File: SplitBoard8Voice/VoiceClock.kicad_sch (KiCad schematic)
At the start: 24 parts, among them U1001 74HC595, U1002 74HC595, U1003 4017, U1004 4017, U1005 4071

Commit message: 8 voice schematics start
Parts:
- removed JP1001: B17, Jumper:SolderJumper-2_P1.3mm_Bridged_Pad1.0x1.5mm, symbol Jumper:SolderJumper_2_Bridged
- removed JP1002: B16, Jumper:SolderJumper-2_P1.3mm_Open_Pad1.0x1.5mm, symbol Jumper:SolderJumper_2_Open
- removed U1001: 74HC595, Package_SO:SOIC-16_3.9x9.9mm_P1.27mm, symbol 74xx:74HC595
- removed U1003, U1004: 4017, Package_SO:SOIC-16_3.9x9.9mm_P1.27mm, symbol 4xxx:4017
- removed U1005: 4071, Package_SO:SOIC-14_3.9x8.7mm_P1.27mm, symbol 4xxx:4071
- added R1013, R1014, R1015, R1016: 22R, Resistor_SMD:R_0805_2012Metric, symbol Device:R_US
- added U1001, U1003: 4013, symbol 4xxx:4013
- added U1004: 74LS08, symbol 74xx:74LS08
- added U1005: 74HC595, Package_SO:SOIC-16_3.9x9.9mm_P1.27mm, symbol 74xx:74HC595
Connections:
- net +3.3V: now also U1001.14 (VDD), U1003.14 (VDD), U1004.14 (VCC), U1005.10 (~{SRCLR}), U1005.16 (VCC)
- net GND: now also U1001.6 (S), U1001.7 (VSS), U1001.8 (S), U1003.6 (S), U1003.7 (VSS), U1004.7 (GND), U1005.13 (~{OE}), U1005.8 (GND)
- net PITCH_MOSI: now also U1004.12, U1004.4; no longer U1002.14 (SER)
- net PITCH_RST_GPIO: now also U1001.10 (R), U1001.4 (R), U1003.4 (R)
- net PITCH_SCK: now also U1001.3 (C), U1004.1, U1004.9; no longer U1002.11 (SRCLK)
- net V1_CLK1: now also R1016.2; no longer R1011.2
- net V1_CLK2: now also R1015.2; no longer R1010.2
- net V2_CLK1: now also R1014.2; no longer R1012.2
- net V2_CLK2: now also R1013.2; no longer R1009.2
- net V3_CLK1: now also R1012.2; no longer R1008.2
- net V3_CLK2: now also R1011.2; no longer R1007.2
- net V4_CLK1: now also R1010.2; no longer R1006.2
- net V4_CLK2: now also R1009.2; no longer R1005.2
- net V5_CLK1: now also R1008.2; no longer R1004.2
- net V5_CLK2: now also R1007.2; no longer R1003.2
- net V6_CLK1: now also R1006.2; no longer R1002.2
- net V6_CLK2: now also R1005.2; no longer R1001.2
- net at R1011.1: now also U1005.2 (QC)
- net at R1009.1: now also U1005.15 (QA)
- net at R1012.1: now also U1005.3 (QD)
- net at R1010.1: now also U1005.1 (QB)
- net PITCH_SS renamed SR1_LATCH
- net SR1_LATCH: now also U1003.2 (~{Q}), U1003.5 (D), U1004.10, U1004.13
- new net: U1001.13 (Q), U1003.3 (C)
- new net: U1001.1 (Q), U1001.11 (C)
- new net: U1001.2 (~{Q}), U1001.5 (D)
- new net: R1013.1, U1005.4 (QE)
- new net: R1014.1, U1005.5 (QF)
- new net: R1015.1, U1005.6 (QG)
- new net: R1016.1, U1005.7 (QH)
- new net: U1001.12 (~{Q}), U1001.9 (D)
- new net SR1_SCK: U1002.11 (SRCLK), U1004.3
- new net SR1_SER: U1002.14 (SER), U1004.6
- new net SR2_LATCH: U1003.1 (Q), U1004.2, U1004.5, U1005.12 (RCLK)
- new net SR2_SCK: U1004.8, U1005.11 (SRCLK)
- new net SR2_SER: U1004.11, U1005.14 (SER)
- new net V7_CLK1: R1004.2
- new net V7_CLK2: R1003.2
- new net V8_CLK1: R1002.2
- new net V8_CLK2: R1001.2
- no-connect marks 21 -> 8
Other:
- note added: "Latch Pin driver/clock mux"
- note added: "Note: the first rising edge on SCK should set all three flip-flops high, which means SR2_LATCH will be high for the first 8 bits"
- note removed: "Hardware Chip Select Driver"
- note removed: "I think I've reasoned through this correcly, but if not we have this solder jumper."
- moved on the sheet: C1002, R1001, R1002, R1003, R1004, R1005, R1006, R1007, U1002

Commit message: galaxy brain clock logic circuit
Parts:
- removed U1001, U1003: 4013, symbol 4xxx:4013
- added C1006, C1007: 100n, Capacitor_SMD:C_0805_2012Metric, symbol Device:C
- added R1017: LOOP, Resistor_THT:R_Axial_DIN0204_L3.6mm_D1.6mm_P5.08mm_Horizontal, symbol Device:R_US
- added TP1001: PITCH_MOSI, TestPoint:TestPoint_THTPad_D1.0mm_Drill0.5mm_VAL, symbol Connector:TestPoint
- added TP1002: SR1_SCK, TestPoint:TestPoint_THTPad_D1.0mm_Drill0.5mm_VAL, symbol Connector:TestPoint
- added TP1003: PITCH_SCK, TestPoint:TestPoint_THTPad_D1.0mm_Drill0.5mm_VAL, symbol Connector:TestPoint
- added TP1004: SR1_SER, TestPoint:TestPoint_THTPad_D1.0mm_Drill0.5mm_VAL, symbol Connector:TestPoint
- added TP1005: SR1_LATCH, TestPoint:TestPoint_THTPad_D1.0mm_Drill0.5mm_VAL, symbol Connector:TestPoint
- added TP1006: SR2_LATCH, TestPoint:TestPoint_THTPad_D1.0mm_Drill0.5mm_VAL, symbol Connector:TestPoint
- added TP1007: SR2_SCK, TestPoint:TestPoint_THTPad_D1.0mm_Drill0.5mm_VAL, symbol Connector:TestPoint
- added TP1008: SR2_SER, TestPoint:TestPoint_THTPad_D1.0mm_Drill0.5mm_VAL, symbol Connector:TestPoint
- added U1001, U1003: 74HC74, Package_SO:SOIC-14_3.9x8.7mm_P1.27mm, symbol 74xx:74HC74
- added U1006, U1007: 74HC14, symbol 74xx:74HC14
- U1004: value 74LS08 -> 74HC08; footprint (none) -> Package_SO:SOIC-14_3.9x8.7mm_P1.27mm
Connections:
- net +3.3V: now also C1006.1, C1007.1, U1001.10 (~{S}), U1001.14 (VCC), U1001.4 (~{S}), U1003.10 (~{S}), U1003.14 (VCC), U1003.4 (~{S}), U1006.14 (VCC), U1007.14 (VCC)
- net GND: now also C1006.2, C1007.2, R1017.1, R1017.2, U1001.7 (GND), U1003.7 (GND), U1006.7 (GND), U1007.7 (GND)
- net PITCH_MOSI: now also TP1001.1, U1007.1; no longer U1004.12, U1004.4
- net PITCH_RST_GPIO: now also U1001.1 (~{R}), U1001.13 (~{R}), U1003.1 (~{R}), U1003.13 (~{R})
- net PITCH_SCK: now also TP1003.1, U1001.3 (C), U1006.1; no longer U1004.1, U1004.9
- net SR1_LATCH: now also TP1005.1, U1003.12 (D), U1003.8 (~{Q})
- net SR1_SCK: now also TP1002.1
- net SR1_SER: now also TP1004.1
- net SR2_LATCH: now also TP1006.1, U1003.9 (Q)
- net SR2_SCK: now also TP1007.1
- net SR2_SER: now also TP1008.1
- new net: U1006.2, U1006.3
- new net: U1006.4, U1006.5
- new net: U1003.2 (D), U1003.6 (~{Q})
- new net: U1001.9 (Q), U1003.3 (C)
- new net: U1003.11 (C), U1003.5 (Q)
- new net: U1007.2, U1007.3
- new net: U1007.4, U1007.5
- new net: U1007.6, U1007.9
- new net: U1001.11 (C), U1001.5 (Q)
- new net: U1001.12 (D), U1001.8 (~{Q})
- new net: U1001.2 (D), U1001.6 (~{Q})
- new net: U1006.6, U1006.9
- new net PITCH_MOSI_DEL: U1004.12, U1004.4, U1007.8
- new net PITCH_SCK_DEL: U1004.1, U1004.9, U1006.8
- no-connect marks 8 -> 10
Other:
- note added: "Note: the first rising edge on SCK should set all four flip-flops high, which means SR2_LATCH will be high for the first 8 bits"
- note removed: "Note: the first rising edge on SCK should set all three flip-flops high, which means SR2_LATCH will be high for the first 8 bits"
- moved on the sheet: C1002, C1004, C1005, R1001, R1002, R1003, R1004, R1005, R1006, R1007, R1009, R1010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

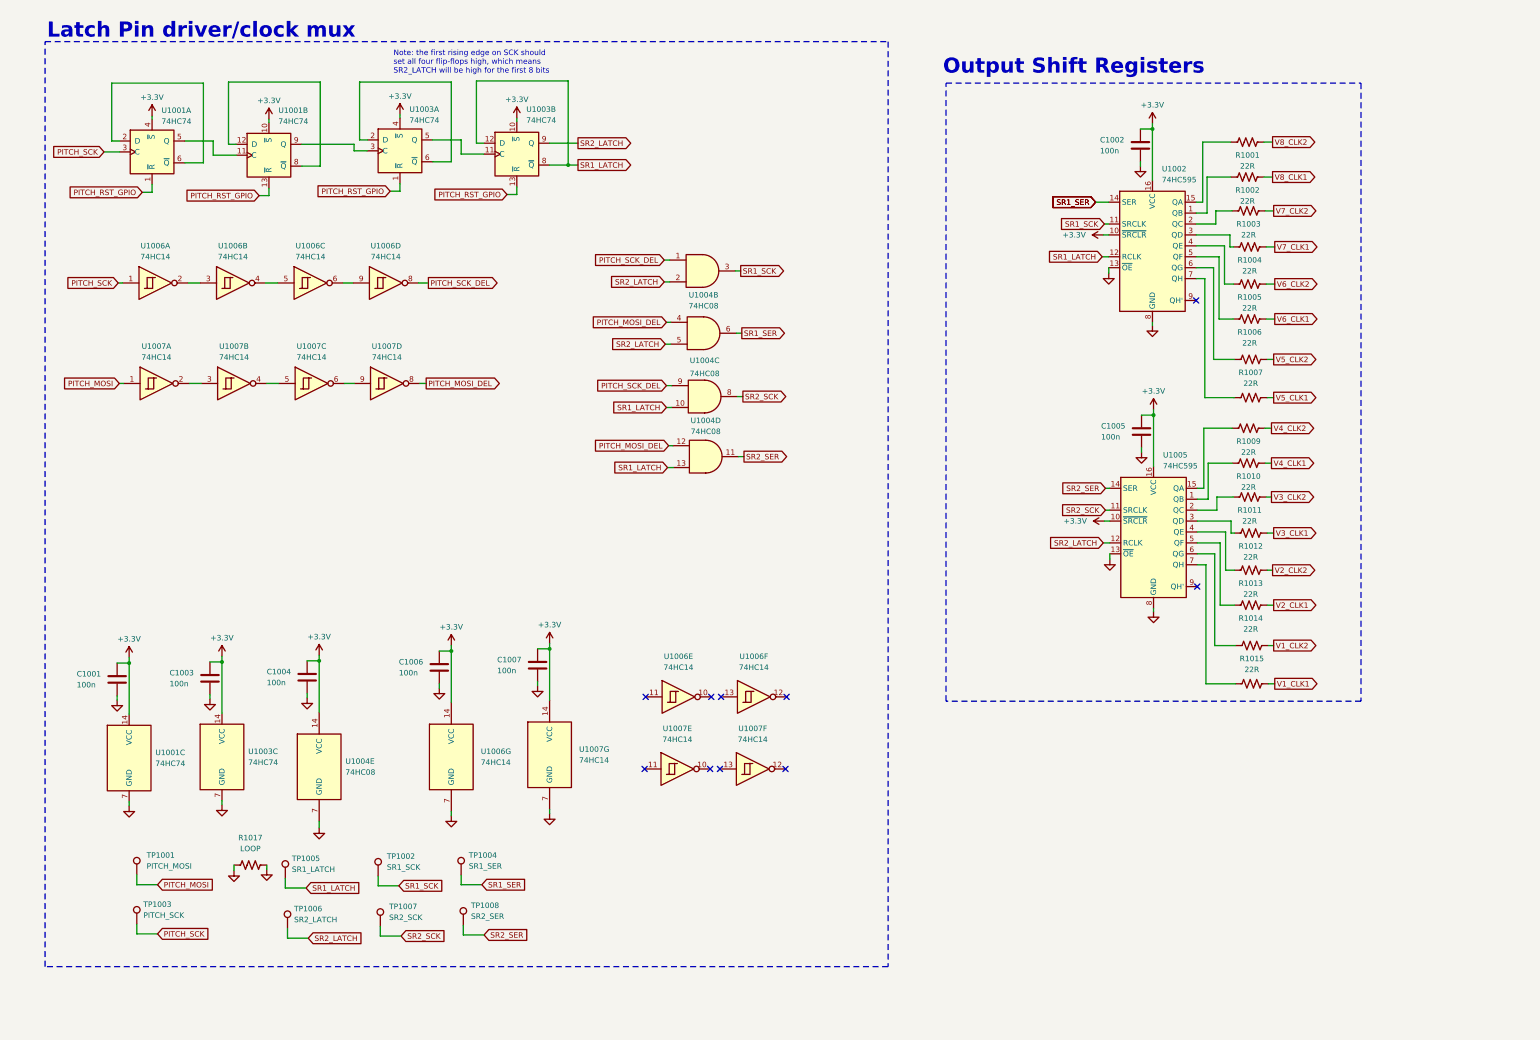
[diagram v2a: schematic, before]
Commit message: added float code for voice clocks
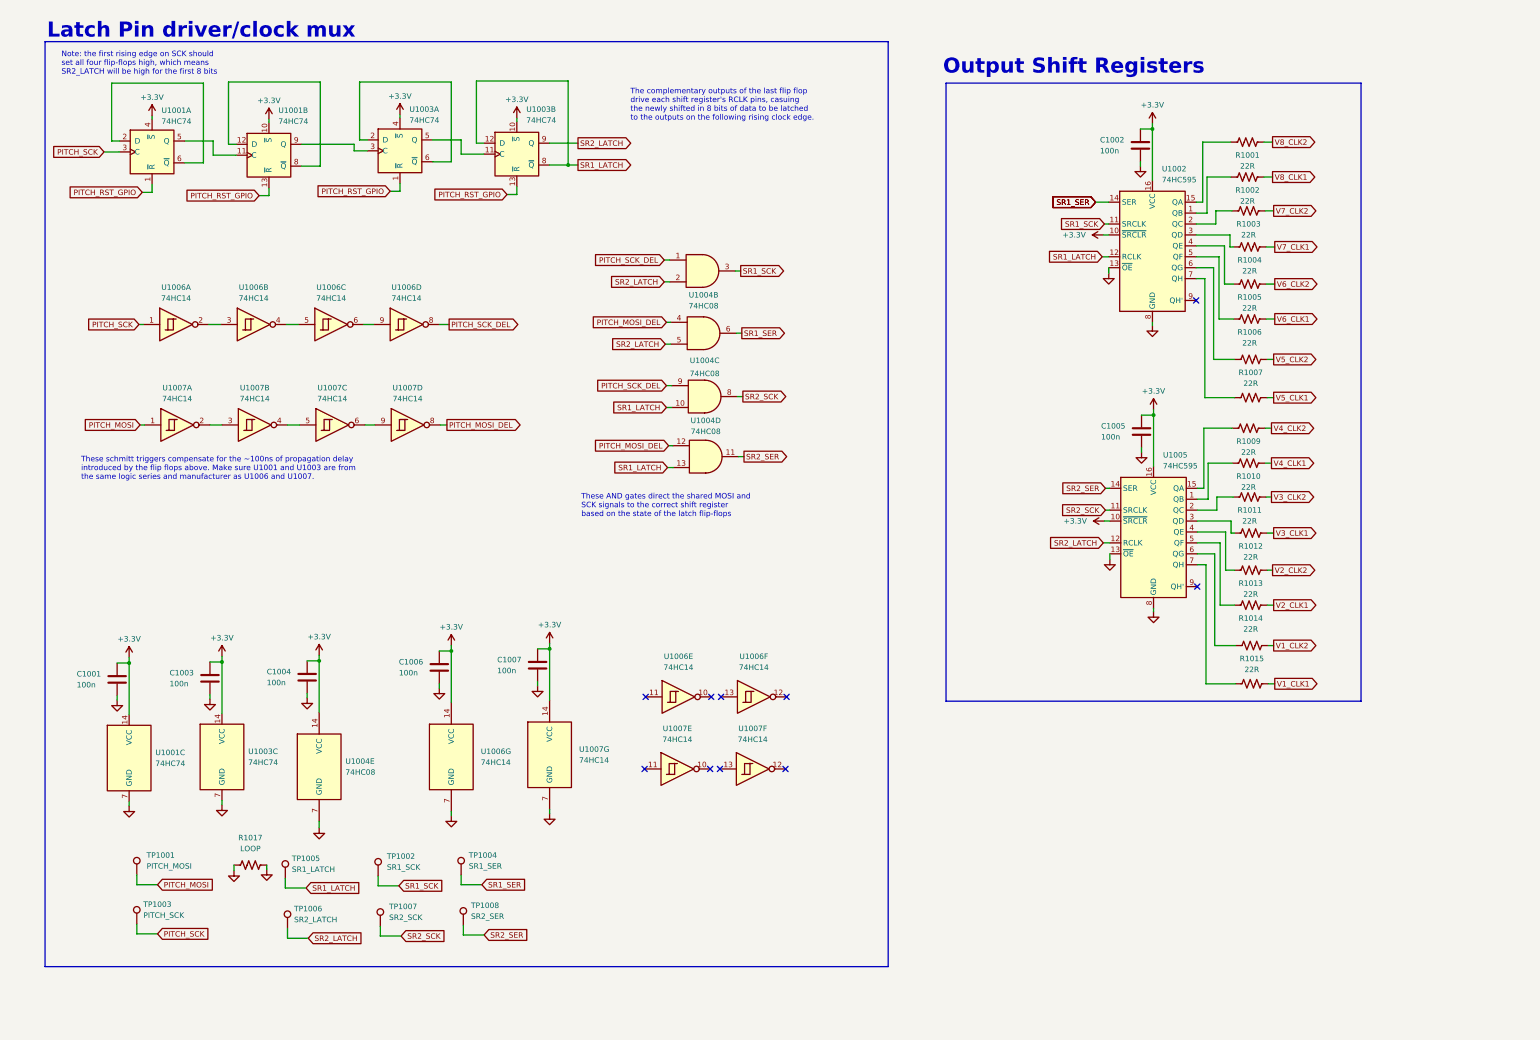
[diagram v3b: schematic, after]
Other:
- note added: "The complementary outputs of the last flip flop drive each shift register's RCLK pins, casuing the newly shifted in 8 bits of data to be latched to the outputs on the following rising clock edge."
- note added: "These AND gates direct the shared MOSI and SCK signals to the correct shift register based on the state of the latch flip-flops"
- note added: "These schmitt triggers compensate for the ~100ns of propagation delay introduced by the flip flops above. Make sure U1001 and U1003 are from the same logic series and manufacturer as U1006 and U1007."
- moved on the sheet: U1006A, U1006B, U1006C, U1006D, U1007A, U1007B, U1007C, U1007D

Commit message: Eurorack power capability sorted out
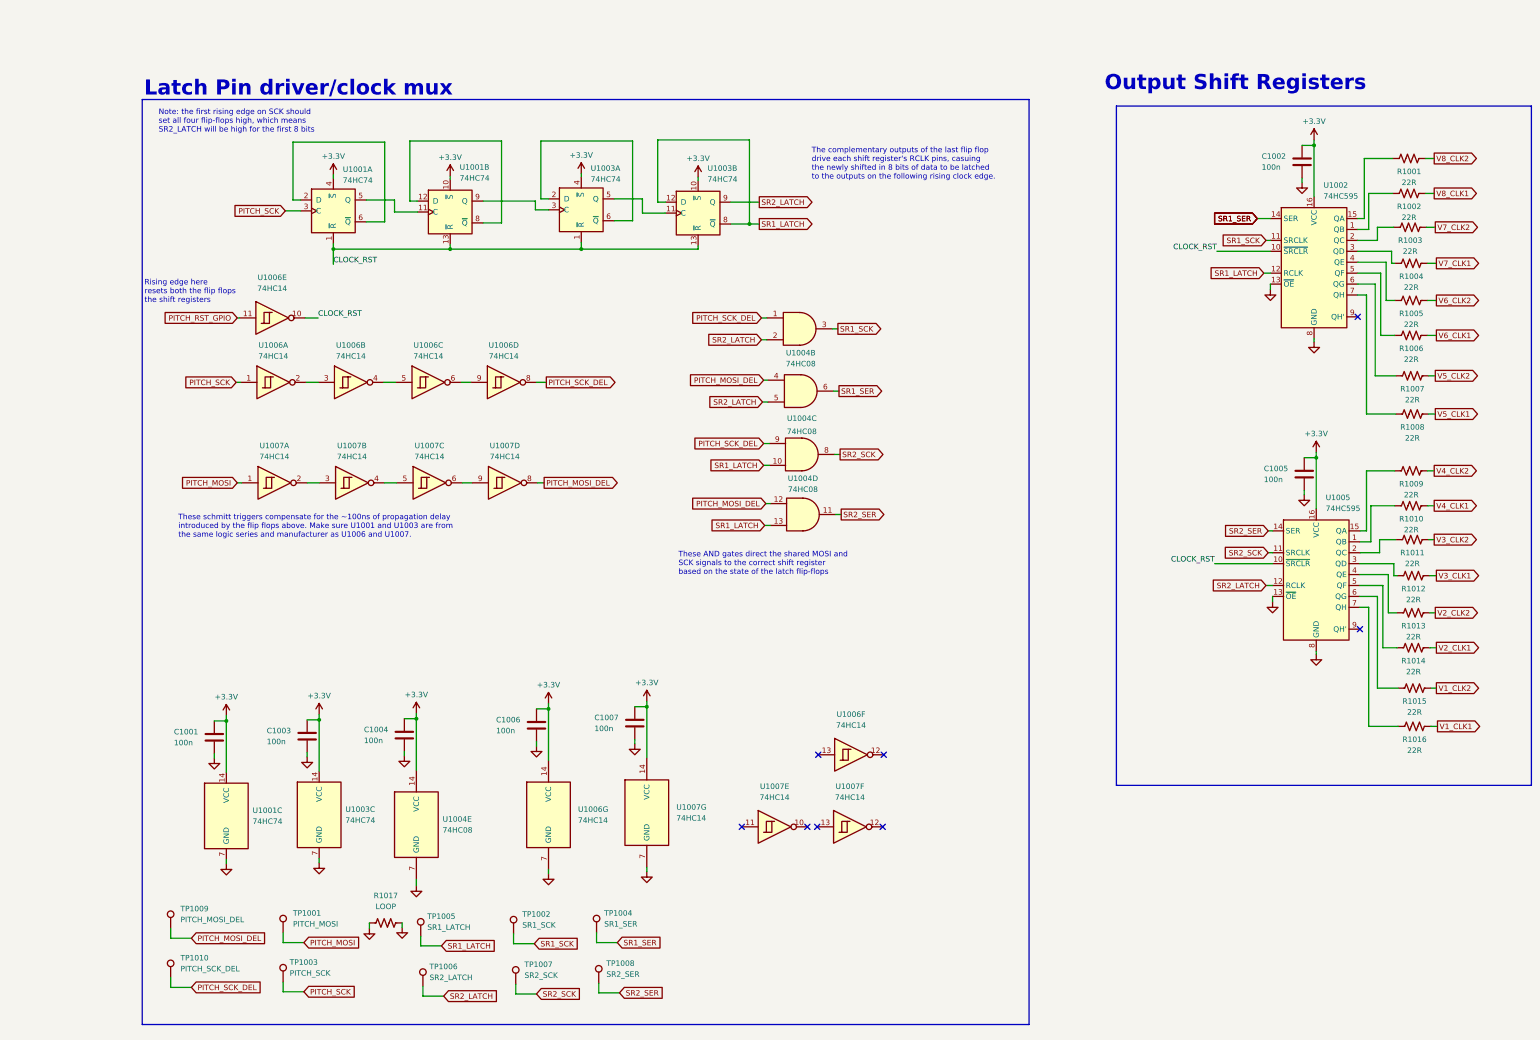
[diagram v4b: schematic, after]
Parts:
- added TP1009: PITCH_MOSI_DEL, TestPoint:TestPoint_THTPad_D1.0mm_Drill0.5mm_VAL, symbol Connector:TestPoint
- added TP1010: PITCH_SCK_DEL, TestPoint:TestPoint_THTPad_D1.0mm_Drill0.5mm_VAL, symbol Connector:TestPoint
- U1006, U1007: footprint (none) -> Package_SO:SOIC-14_3.9x8.7mm_P1.27mm
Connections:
- net +3.3V: no longer U1002.10 (~{SRCLR}), U1005.10 (~{SRCLR})
- net PITCH_MOSI_DEL: now also TP1009.1
- net PITCH_RST_GPIO: now also U1006.11; no longer U1001.1 (~{R}), U1001.13 (~{R}), U1003.1 (~{R}), U1003.13 (~{R})
- net PITCH_SCK_DEL: now also TP1010.1
- net CLOCK_RST: now reaches U1006.10
- net CLOCK_RST: now also U1001.1 (~{R}), U1001.13 (~{R}), U1002.10 (~{SRCLR}), U1003.1 (~{R}), U1003.13 (~{R}), U1005.10 (~{SRCLR})
- no-connect marks 10 -> 8
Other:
- note added: "Rising edge here resets both the flip flops the shift registers"
- moved on the sheet: C1001, C1002, C1003, C1004, C1005, C1006, C1007, R1001, R1002, R1003, R1004, R1005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

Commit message: 8V layout rev1
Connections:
- net PITCH_MOSI_DEL: now also U1004.9; no longer U1004.12
- net PITCH_SCK_DEL: now also U1004.12; no longer U1004.9
- net SR1_LATCH: now also U1004.2, U1004.5; no longer U1004.10, U1004.13
- net SR1_SCK: now also U1004.11; no longer U1004.3
- net SR1_SER: now also U1004.8; no longer U1004.6
- net SR2_LATCH: now also U1004.10, U1004.13; no longer U1004.2, U1004.5
- net SR2_SCK: now also U1004.3; no longer U1004.8
- net SR2_SER: now also U1004.6; no longer U1004.11
- net at R1009.1: now also U1005.7 (QH); no longer U1005.15 (QA)
- net at R1012.1: now also U1005.4 (QE); no longer U1005.3 (QD)
- net at R1004.1: now also U1002.4 (QE); no longer U1002.3 (QD)
- net at R1008.1: now also U1002.15 (QA); no longer U1002.7 (QH)
- net at R1007.1: now also U1002.1 (QB); no longer U1002.6 (QG)
- net at R1003.1: now also U1002.5 (QF); no longer U1002.2 (QC)
- net at U1005.1 (QB): now also R1015.1; no longer R1010.1
- net at U1005.2 (QC): now also R1014.1; no longer R1011.1
- net at R1013.1: now also U1005.3 (QD); no longer U1005.4 (QE)
- net at U1005.5 (QF): now also R1011.1; no longer R1014.1
- net at U1005.6 (QG): now also R1010.1; no longer R1015.1
- net at R1016.1: now also U1005.15 (QA); no longer U1005.7 (QH)
- net at R1005.1: now also U1002.3 (QD); no longer U1002.4 (QE)
- net at R1006.1: now also U1002.2 (QC); no longer U1002.5 (QF)
- net at R1001.1: now also U1002.7 (QH); no longer U1002.15 (QA)
- net at R1002.1: now also U1002.6 (QG); no longer U1002.1 (QB)
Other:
- moved on the sheet: R1001, R1002, R1003, R1004, R1005, R1006, R1007, R1008, R1009, R1010, R1011, R1012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
